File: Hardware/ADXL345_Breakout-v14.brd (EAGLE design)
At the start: 20.3 x 15.2 mm, 10 parts, among them U2 ADXL345PATRICK

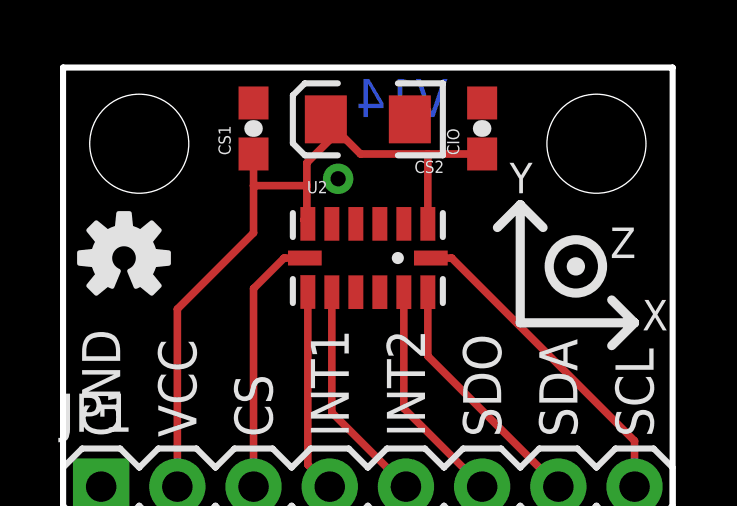
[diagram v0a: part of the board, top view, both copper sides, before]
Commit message: Moved OSH logo, cleaned up routes
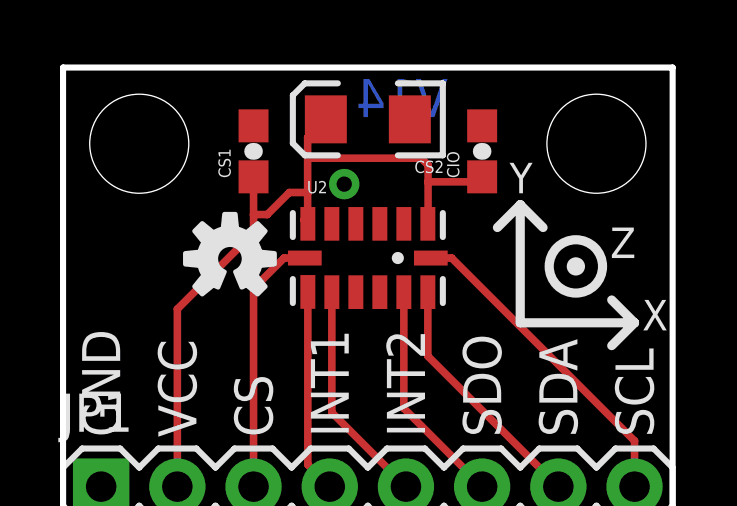
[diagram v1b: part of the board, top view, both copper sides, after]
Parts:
- moved U$3 3.53 mm to (5.56, 8.86)
- moved CIO 0.76 mm to (14.0, 12.4)
- moved CS1 0.76 mm to (6.35, 12.4)
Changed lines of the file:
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@@
 <layer number="27" name="tValues" color="7" fill="1" visible="no" active="yes"/>
 <layer number="28" name="bValues" color="7" fill="1" visible="no" active="yes"/>
-<layer number="29" name="tStop" color="7" fill="3" visible="yes" active="yes"/>
+<layer number="29" name="tStop" color="7" fill="3" visible="no" active="yes"/>
 <layer number="30" name="bStop" color="7" fill="6" visible="no" active="yes"/>
 <layer number="31" name="tCream" color="7" fill="4" visible="no" active="yes"/>
@@
 <element name="JP1" library="SparkFun" package="1X08" value="" x="1.27" y="1.27"/>
 <element name="U$2" library="SparkFun" package="SFE-NEW-WEBLOGO" value="LOGO-SFENEW" x="19.685" y="7.874" rot="MR0"/>
-<element name="CS1" library="SparkFun" package="0603-CAP" value="0.1uF" x="6.35" y="13.208" rot="R90"/>
-<element name="CIO" library="SparkFun" package="0603-CAP" value="0.1uF" x="13.97" y="13.208" rot="R90"/>
+<element name="CS1" library="SparkFun" package="0603-CAP" value="0.1uF" x="6.35" y="12.446" rot="R90"/>
+<element name="CIO" library="SparkFun" package="0603-CAP" value="0.1uF" x="13.97" y="12.446" rot="R90"/>
 <element name="CS2" library="SparkFun" package="EIA3216" value="10uF" x="10.16" y="13.5128" rot="R180"/>
 <element name="JP2" library="SparkFun" package="STAND-OFF" value="STAND-OFF" x="2.54" y="12.7"/>
 <element name="JP3" library="SparkFun" package="STAND-OFF" value="STAND-OFF" x="17.78" y="12.7"/>
 <element name="U$1" library="SparkFun" package="CREATIVE_COMMONS" value="CREATIVE_COMMONS" x="0" y="-7.62"/>
-<element name="U$3" library="SparkFun-Aesthetics" package="OSHW-LOGO-S" value="OSHW-LOGOS" x="2.032" y="8.89"/>
+<element name="U$3" library="SparkFun-Aesthetics" package="OSHW-LOGO-S" value="OSHW-LOGOS" x="5.5626" y="8.8646"/>
 <element name="U2" library="Testing" package="LGA14_1:1_PATRICK" value="ADXL345PATRICK" x="10.16" y="8.89"/>
 </elements>
@@
 <contactref element="U2" pad="5"/>
 <contactref element="U2" pad="2"/>
-<via x="9.1694" y="11.5316" extent="1-16" drill="0.508"/>
+<via x="9.3726" y="11.3538" extent="1-16" drill="0.508"/>
 </signal>
 <signal name="CS">
@@
 <contactref element="U2" pad="1"/>
 <contactref element="U2" pad="6"/>
-<wire x1="6.35" y1="11.303" x2="6.35" y2="12.358" width="0.254" layer="1"/>
 <wire x1="8.16" y1="10.0281" x2="8.0281" y2="10.16" width="0.254" layer="1"/>
-<wire x1="8.0281" y1="10.16" x2="8.128" y2="10.2599" width="0.254" layer="1"/>
-<wire x1="13.97" y1="12.358" x2="12.16" y2="12.358" width="0.254" layer="1"/>
-<wire x1="12.16" y1="12.358" x2="9.9148" y2="12.358" width="0.254" layer="1"/>
-<wire x1="9.9148" y1="12.358" x2="9.1044" y2="13.1684" width="0.254" layer="1"/>
-<wire x1="9.1044" y1="13.1684" x2="8.76" y2="13.5128" width="0.254" layer="1"/>
-<wire x1="12.16" y1="10.0281" x2="12.16" y2="12.358" width="0.254" layer="1"/>
+<wire x1="8.0281" y1="10.16" x2="8.1534" y2="10.2853" width="0.254" layer="1"/>
 <wire x1="3.81" y1="1.27" x2="3.81" y2="7.1882" width="0.254" layer="1"/>
 <wire x1="3.81" y1="7.1882" x2="6.35" y2="9.7282" width="0.254" layer="1"/>
-<wire x1="9.1044" y1="13.1684" x2="9.1044" y2="13.0414" width="0.254" layer="1"/>
-<wire x1="9.1044" y1="13.0414" x2="8.128" y2="12.065" width="0.254" layer="1"/>
-<wire x1="8.128" y1="12.065" x2="8.128" y2="11.303" width="0.254" layer="1"/>
-<wire x1="8.128" y1="11.303" x2="8.128" y2="10.0601" width="0.254" layer="1"/>
-<wire x1="8.128" y1="10.0601" x2="8.16" y2="10.0281" width="0.254" layer="1"/>
-<wire x1="6.35" y1="9.7282" x2="6.35" y2="11.303" width="0.254" layer="1"/>
-<wire x1="6.35" y1="11.303" x2="8.128" y2="11.303" width="0.254" layer="1"/>
+<wire x1="6.35" y1="10.3378" x2="6.35" y2="11.596" width="0.254" layer="1"/>
+<wire x1="8.763" y1="13.5098" x2="8.76" y2="13.5128" width="0.254" layer="1"/>
+<wire x1="12.192" y1="10.0601" x2="12.16" y2="10.0281" width="0.254" layer="1"/>
+<wire x1="6.4652" y1="11.4808" x2="6.35" y2="11.596" width="0.254" layer="1"/>
+<wire x1="6.4652" y1="11.4808" x2="6.4652" y2="11.43" width="0.254" layer="1"/>
+<wire x1="12.1666" y1="11.9888" x2="12.1666" y2="11.43" width="0.254" layer="1"/>
+<wire x1="12.1666" y1="11.43" x2="12.1666" y2="10.0347" width="0.254" layer="1"/>
+<wire x1="12.1666" y1="10.0347" x2="12.16" y2="10.0281" width="0.254" layer="1"/>
+<wire x1="13.97" y1="11.596" x2="13.804" y2="11.43" width="0.254" layer="1"/>
+<wire x1="13.804" y1="11.43" x2="12.1666" y2="11.43" width="0.254" layer="1"/>
+<wire x1="8.76" y1="13.1288" x2="8.76" y2="13.5128" width="0.254" layer="1"/>
+<wire x1="12.1666" y1="11.9888" x2="11.938" y2="12.2174" width="0.254" layer="1"/>
+<wire x1="11.938" y1="12.2174" x2="8.1534" y2="12.2174" width="0.254" layer="1"/>
+<wire x1="8.1534" y1="10.2853" x2="8.1534" y2="11.049" width="0.254" layer="1"/>
+<wire x1="8.1534" y1="11.049" x2="8.1534" y2="12.2174" width="0.254" layer="1"/>
+<wire x1="8.1534" y1="12.2174" x2="8.1534" y2="12.9062" width="0.254" layer="1"/>
+<wire x1="8.1534" y1="12.9062" x2="8.76" y2="13.5128" width="0.254" layer="1"/>
+<wire x1="6.35" y1="9.7282" x2="6.35" y2="10.3378" width="0.254" layer="1"/>
+<wire x1="6.35" y1="10.3378" x2="6.8072" y2="10.3378" width="0.254" layer="1"/>
+<wire x1="6.8072" y1="10.3378" x2="7.5438" y2="11.0744" width="0.254" layer="1"/>
+<wire x1="7.5438" y1="11.0744" x2="8.128" y2="11.0744" width="0.254" layer="1"/>
+<wire x1="8.128" y1="11.0744" x2="8.1534" y2="11.049" width="0.254" layer="1"/>
 </signal>
 </signals>

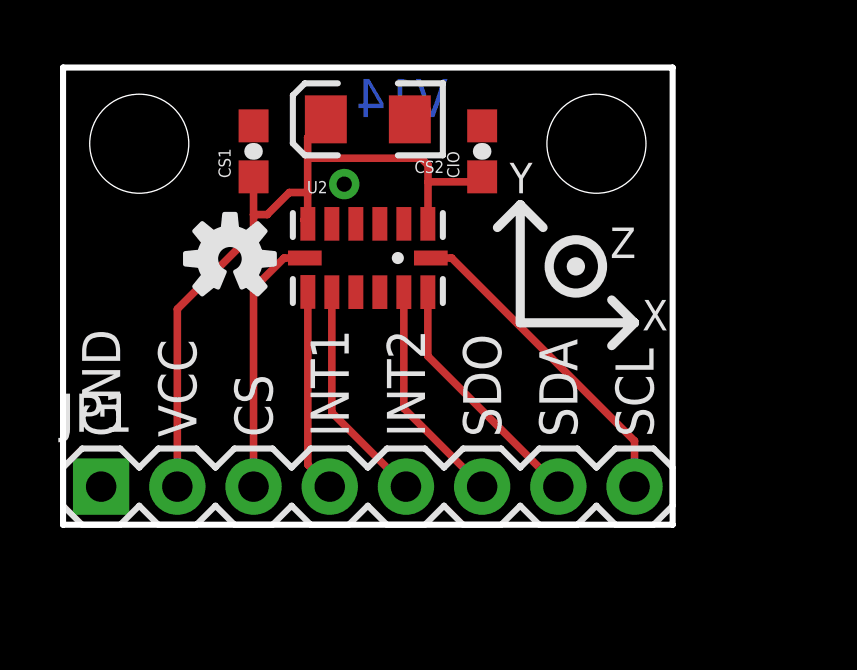
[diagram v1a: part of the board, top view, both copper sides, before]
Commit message: Schematic Change, CAP Names, Package Move
Updated to Frame Letter for the Schematic, Changed Caps names to C2, C1
and Moved the ADXL345 package to make more room for the 10uf Cap.
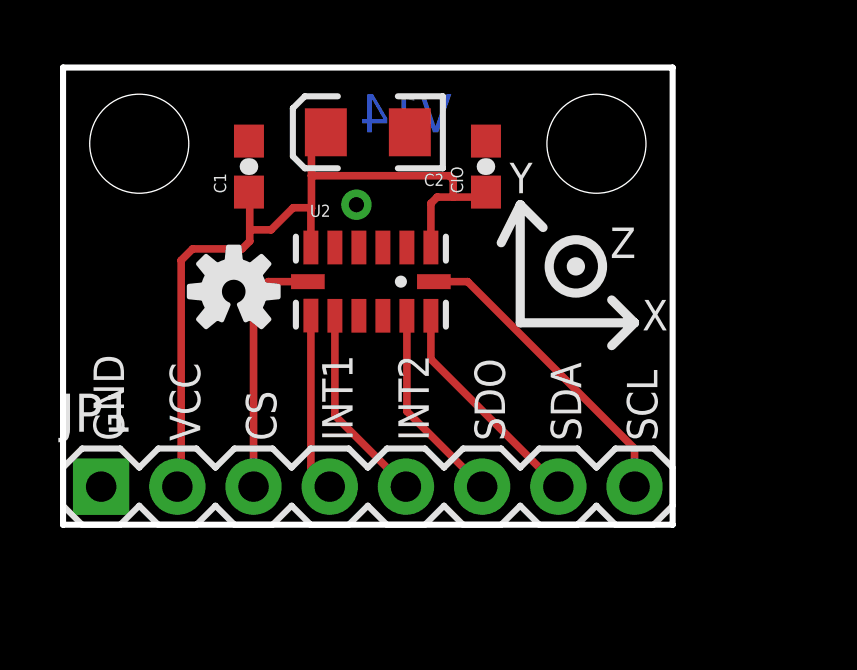
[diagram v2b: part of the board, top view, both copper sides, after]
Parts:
- removed CS1: 0.1uF, SparkFun:0603-CAP
- removed CS2: 10uF, SparkFun:EIA3216
- removed U$1: CREATIVE_COMMONS, SparkFun:CREATIVE_COMMONS
- added C1: 0.1uF, SparkFun:0603-CAP
- added C2: 10uF, SparkFun:EIA3216
- moved U$3 1.10 mm to (5.69, 7.77)
- moved U2 0.79 mm to (10.3, 8.10)
- moved CIO 0.52 mm to (14.1, 11.9)
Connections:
- net GND: now also C1.2, C2.C; no longer CS1.2, CS2.C
- net VCC: now also C1.1, C2.A; no longer CS1.1, CS2.A
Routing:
- net VCC: track 25.9 -> 27.4 mm
- net SDO: track 7.56 -> 6.73 mm
- net INT1: track 6.79 -> 5.96 mm
- net SDA: track 8.28 -> 7.45 mm
- net INT2: track 7.51 -> 6.68 mm
- net SCL: track 10.8 -> 10.3 mm

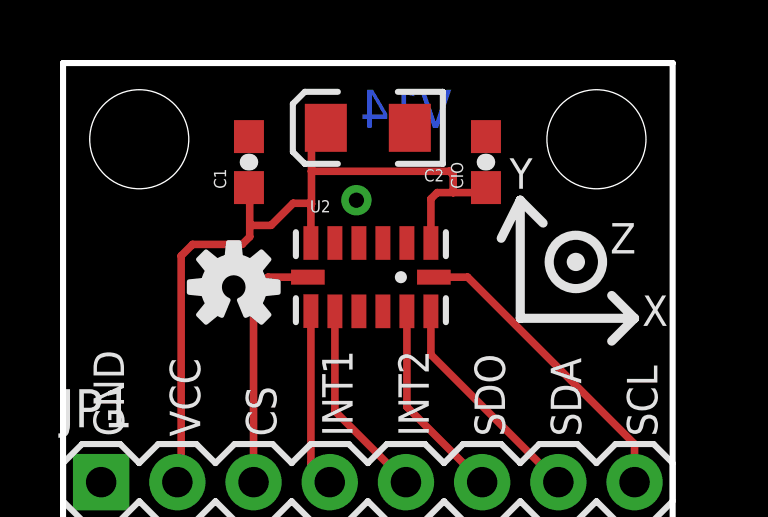
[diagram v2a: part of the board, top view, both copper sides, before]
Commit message: Added fiducials
Forgot to put these on the protos, fiducials now added.
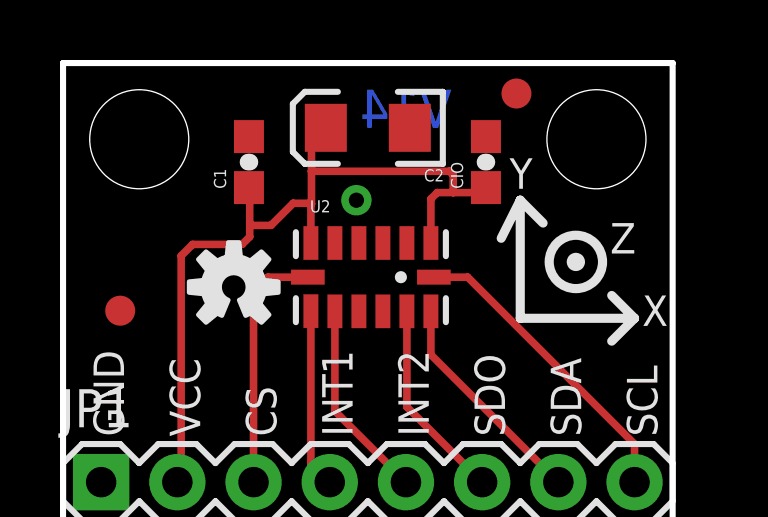
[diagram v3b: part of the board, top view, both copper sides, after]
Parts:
- added JP4, JP5: FIDUCIAL1X2, SparkFun-Aesthetics:FIDUCIAL-1X2
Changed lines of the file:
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@@
 <layer number="27" name="tValues" color="7" fill="1" visible="no" active="yes"/>
 <layer number="28" name="bValues" color="7" fill="1" visible="no" active="yes"/>
-<layer number="29" name="tStop" color="7" fill="3" visible="no" active="yes"/>
+<layer number="29" name="tStop" color="7" fill="3" visible="yes" active="yes"/>
 <layer number="30" name="bStop" color="7" fill="6" visible="no" active="yes"/>
 <layer number="31" name="tCream" color="7" fill="4" visible="no" active="yes"/>
@@
 <element name="U$3" library="SparkFun-Aesthetics" package="OSHW-LOGO-S" value="OSHW-LOGOS" x="5.6896" y="7.7724"/>
 <element name="U2" library="Testing" package="LGA14_1:1_PATRICK" value="ADXL345PATRICK" x="10.2616" y="8.1026"/>
+<element name="JP4" library="SparkFun-Aesthetics" package="FIDUCIAL-1X2" value="FIDUCIAL1X2" x="1.905" y="6.985"/>
+<element name="JP5" library="SparkFun-Aesthetics" package="FIDUCIAL-1X2" value="FIDUCIAL1X2" x="15.113" y="14.224"/>
 </elements>
 <signals>
